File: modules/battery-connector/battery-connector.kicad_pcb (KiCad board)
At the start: 2 copper layers, 1 part, among them J1 691210910002

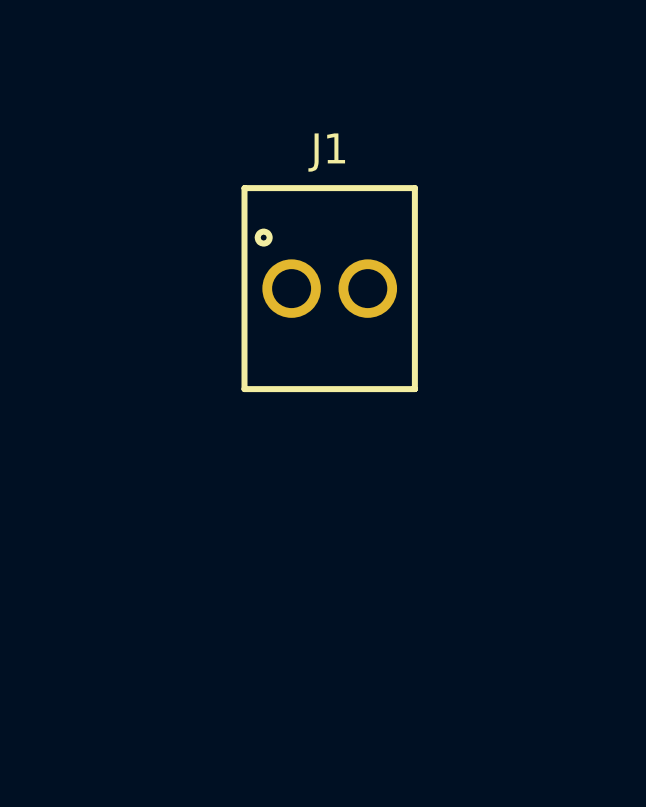
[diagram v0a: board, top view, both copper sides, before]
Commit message: finish battery connector module design
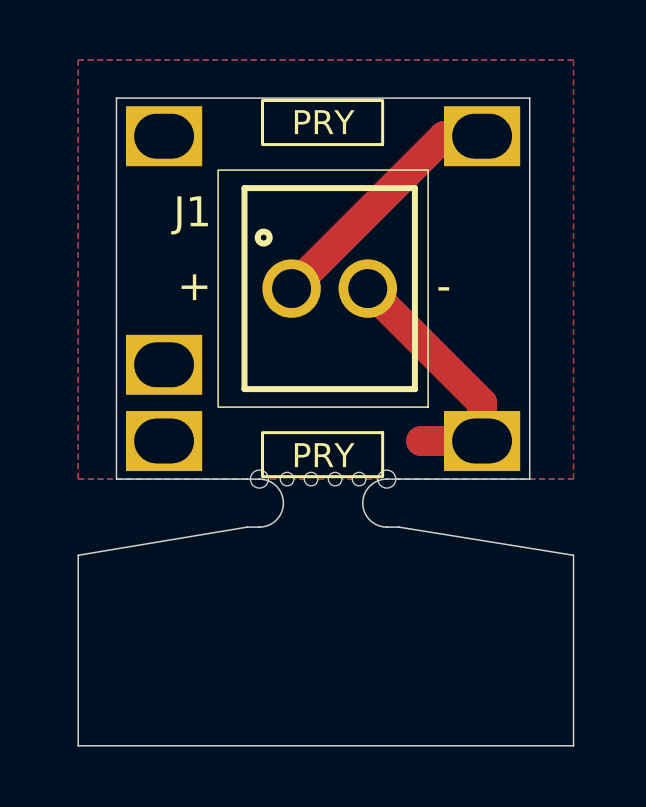
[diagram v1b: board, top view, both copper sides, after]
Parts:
- added M1: ~, MegaCastle:MegaCastle2x5-Module-I7.0x7.9-M8CC-PANEL-NIBBLE, B.Cu at (67.9, 61.0)
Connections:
- J1 pad 1: unconnected-(J1-Pad1) -> VBAT_+
- J1 pad 2: unconnected-(J1-Pad2) -> VBAT_-
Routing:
- net VBAT_-: track 0.00 -> 10.7 mm
- net VBAT_+: track 0.00 -> 8.45 mm
- added copper zone on B.Cu, net VBAT_-
- added copper zone on F.Cu, net VBAT_-
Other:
- board outline added: 13.8 x 14.3 mm
- board text added: "+"
- board text added: "-"
- board text added: "R20250405"

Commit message: KiCad v9 adding new footprints
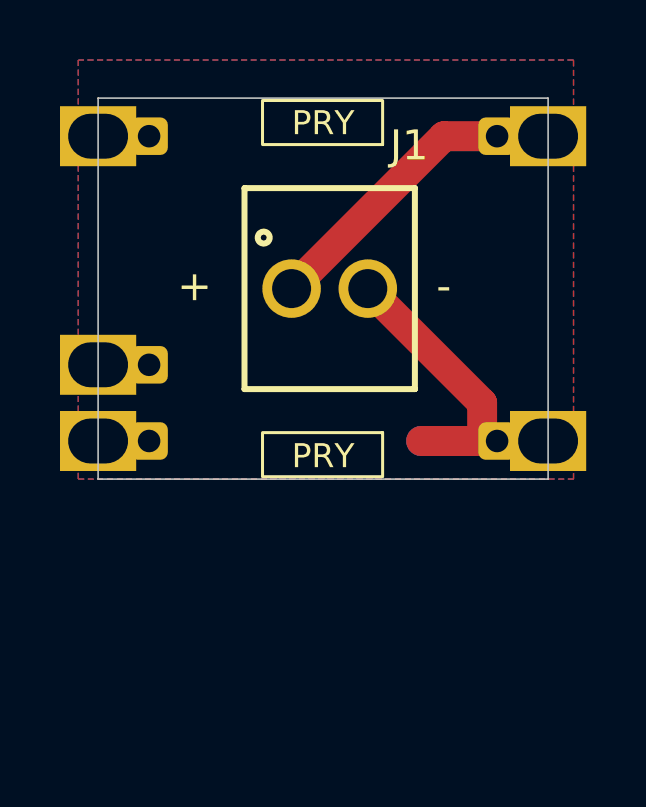
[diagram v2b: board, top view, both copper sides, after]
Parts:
- J1: footprint footprints:691210910002 -> MegaCastle:691210910002
- M1: footprint MegaCastle:MegaCastle2x5-Module-I7.0x7.9-M8CC-PANEL-NIBBLE -> MegaCastle:MegaCastle2x5-Module-I15.0x7.9-M8CC-SPAREPAD
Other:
- board size 13.8 x 14.3 mm -> 15 x 12.7 mm
